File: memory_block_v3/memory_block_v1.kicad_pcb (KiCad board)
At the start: 4 copper layers, 43.8 x 68.2 mm, 19 parts, among them J1 4677, J2 DM3D-SF, J3 Conn_02x04_Odd_Even, J4 Conn_01x19, J5 Conn_01x04, J6 Conn_01x19, J7 Conn_02x06_Top_Bottom, U1 ESP32-WROOM-32E-N8, U2 W25Q128JVSIQ TR

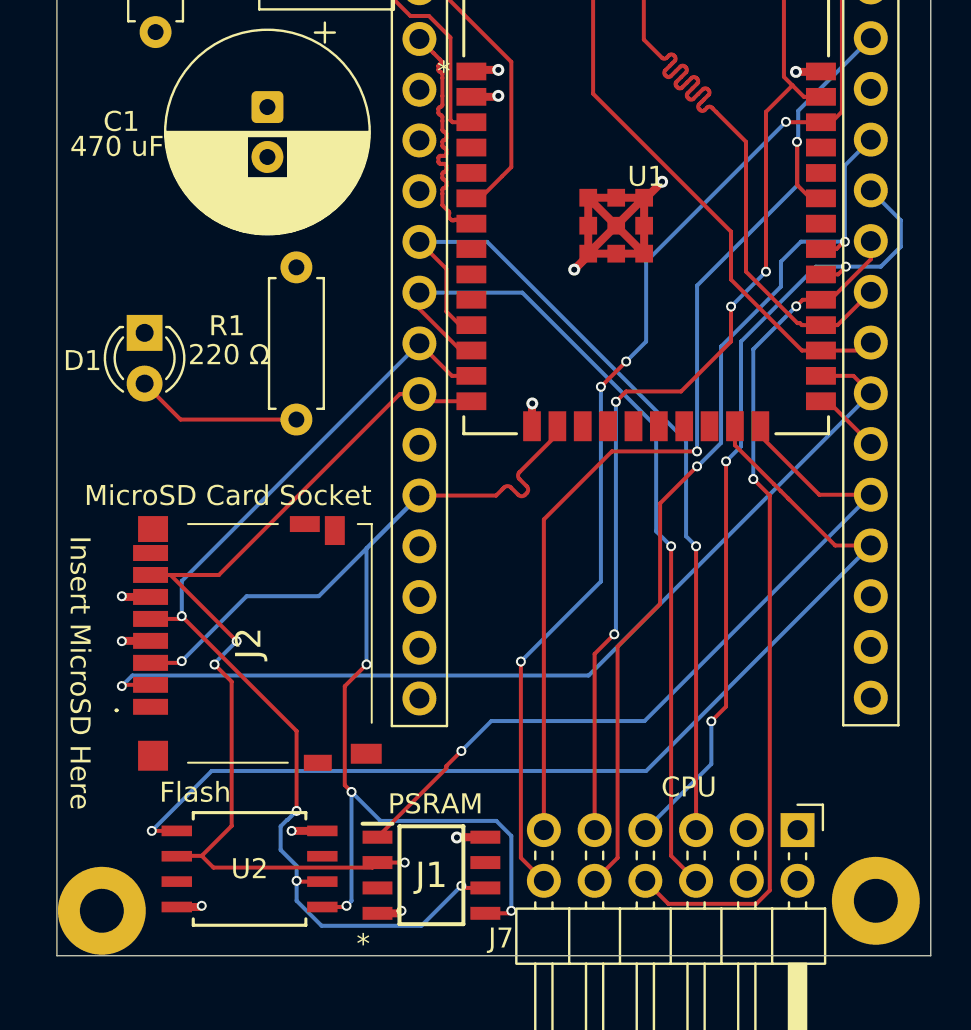
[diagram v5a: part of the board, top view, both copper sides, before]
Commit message: Final (Electrical) Draft for v3
Trace routing and length matching done. May alter silkscreens, but almost ready.
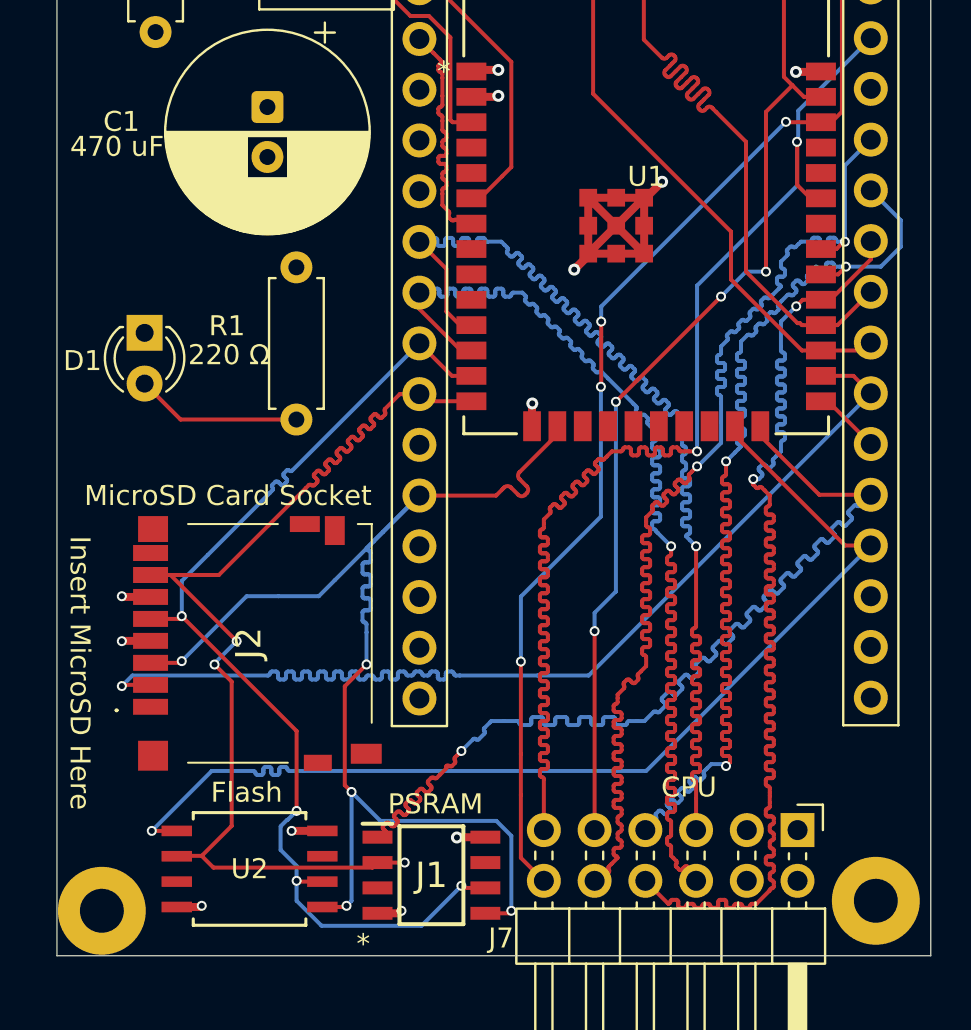
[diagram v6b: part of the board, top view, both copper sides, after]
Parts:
- moved G*** 55.2 mm to (359.1, 303.2), turned to 180 degrees
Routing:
- net CPU_IO0: track 42.8 -> 62.8 mm
- net CPU_IO1: track 42.5 -> 61.7 mm
- net VSPI_CLK: track 41.3 -> 60.0 mm
- net VSPI_CS: track 43.1 -> 61.5 mm
- net VSPI_D1: track 45.5 -> 61.8 mm
- net VSPI_D2: track 52.6 -> 66.7 mm
- net HSPI_CS_PS: track 39.1 -> 52.4 mm
- net HSPI_CS_SD: track 47.9 -> 53.6 mm
- net HSPI_MISO: track 49.9 -> 53.8 mm
- net HSPI_MOSI: track 64.6 -> 66.4 mm
- net VSPI_D0: track 59.2 -> 58.1 mm
- net HSPI_CS_FL: track 53.0 -> 53.9 mm
- net HSPI_CLK: track 52.9 -> 53.8 mm
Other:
- board text added: "{dblquote}I fear not the man who has made 10,000 PCBs once, but I fear the man who has made one PCB 10,000 times.{dblquote}"
